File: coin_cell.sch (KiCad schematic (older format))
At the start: 11 parts, among them J1 Barrel_Jack, U1 NC7SZ14-D, U2 TPS61222

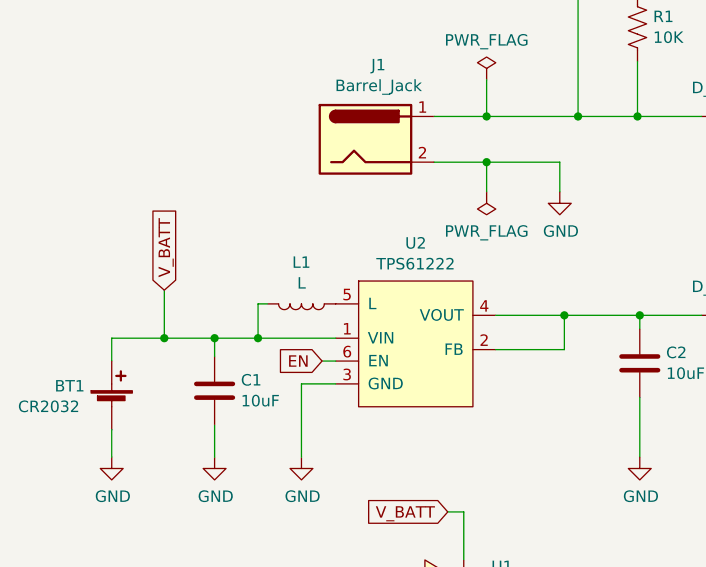
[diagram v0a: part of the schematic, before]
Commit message: Added sc-70-5 footprint and sot23-5 footprint
- assigned footprints to symbols
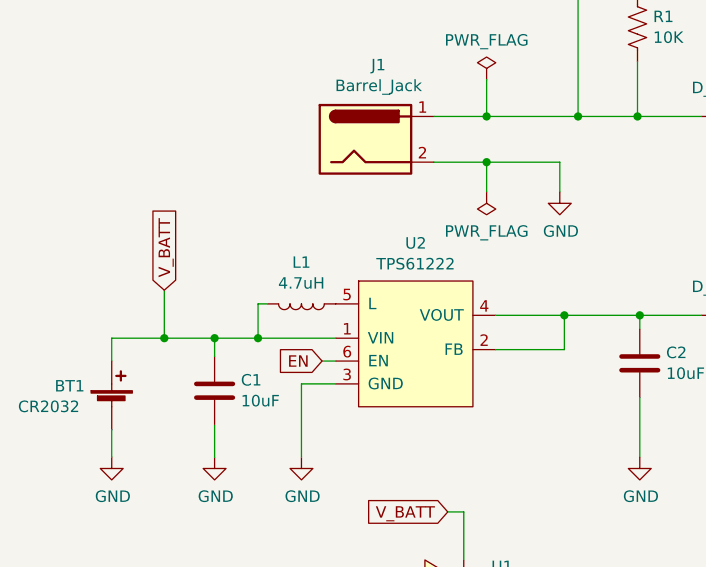
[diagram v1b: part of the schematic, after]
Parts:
- BT1: footprint (none) -> digikey-footprints:Battery_Holder_Coin_2032_BS-7
- C1, C2, C3: footprint (none) -> Capacitor_SMD:C_0805_2012Metric_Pad1.15x1.40mm_HandSolder
- D1, D2: footprint (none) -> Diode_SMD:D_0805_2012Metric_Pad1.15x1.40mm_HandSolder
- J1: footprint (none) -> digikey-footprints:Barrel_Jack_5.5mmODx2.1mmID_PJ-202A
- L1: value L -> 4.7uH; footprint (none) -> Inductor_SMD:L_10.4x10.4_H4.8
- R1: footprint (none) -> Resistor_SMD:R_0805_2012Metric_Pad1.15x1.40mm_HandSolder
- U1: footprint (none) -> coin_cell:SOT-23-5_HandSoldering
- U2: footprint (none) -> Package_TO_SOT_SMD:SOT-363_SC-70-6_Handsoldering
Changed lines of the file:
@@
 EESchema Schematic File Version 4
+LIBS:coin_cell-cache
 EELAYER 29 0
 EELAYER END
@@
 F 0 "U2" H 2620 3385 50  0000 C CNN
 F 1 "TPS61222" H 2620 3294 50  0000 C CNN
-F 2 "" H 2420 2820 50  0001 C CNN
+F 2 "Package_TO_SOT_SMD:SOT-363_SC-70-6_Handsoldering" H 2420 2820 50  0001 C CNN
 F 3 "" H 2420 2820 50  0001 C CNN
 	1    2620 2920
@@
 F 0 "J1" H 2457 2325 50  0000 C CNN
 F 1 "Barrel_Jack" H 2457 2234 50  0000 C CNN
-F 2 "" H 2450 1960 50  0001 C CNN
+F 2 "digikey-footprints:Barrel_Jack_5.5mmODx2.1mmID_PJ-202A" H 2450 1960 50  0001 C CNN
 F 3 "~" H 2450 1960 50  0001 C CNN
 	1    2400 2000
@@
 F 0 "D1" H 4020 1684 50  0000 C CNN
 F 1 "D_Schottky" H 4020 1775 50  0000 C CNN
-F 2 "" H 4020 1900 50  0001 C CNN
+F 2 "Diode_SMD:D_0805_2012Metric_Pad1.15x1.40mm_HandSolder" H 4020 1900 50  0001 C CNN
 F 3 "~" H 4020 1900 50  0001 C CNN
 	1    4020 1900
@@
 F 0 "C2" H 3715 3026 50  0000 L CNN
 F 1 "10uF" H 3715 2935 50  0000 L CNN
-F 2 "" H 3638 2830 50  0001 C CNN
+F 2 "Capacitor_SMD:C_0805_2012Metric_Pad1.15x1.40mm_HandSolder" H 3638 2830 50  0001 C CNN
 F 3 "~" H 3600 2980 50  0001 C CNN
 	1    3600 2980
@@
 P 2120 2720
 F 0 "L1" V 1939 2720 50  0000 C CNN
-F 1 "L" V 2030 2720 50  0000 C CNN
-F 2 "" H 2120 2720 50  0001 C CNN
+F 1 "4.7uH" V 2030 2720 50  0000 C CNN
+F 2 "Inductor_SMD:L_10.4x10.4_H4.8" H 2120 2720 50  0001 C CNN
 F 3 "~" H 2120 2720 50  0001 C CNN
 	1    2120 2720
@@
 F 0 "C1" H 1855 3146 50  0000 L CNN
 F 1 "10uF" H 1855 3055 50  0000 L CNN
-F 2 "" H 1778 2950 50  0001 C CNN
+F 2 "Capacitor_SMD:C_0805_2012Metric_Pad1.15x1.40mm_HandSolder" H 1778 2950 50  0001 C CNN
 F 3 "~" H 1740 3100 50  0001 C CNN
 	1    1740 3100
@@
 F 0 "BT1" H 1040 3260 50  0000 L CNN
 F 1 "CR2032" H 880 3170 50  0000 L CNN
-F 2 "" V 1290 3230 50  0001 C CNN
+F 2 "digikey-footprints:Battery_Holder_Coin_2032_BS-7" V 1290 3230 50  0001 C CNN
 F 3 "~" V 1290 3230 50  0001 C CNN
 	1    1290 3170
@@
 F 0 "D2" H 4020 2554 50  0000 C CNN
 F 1 "D_Schottky" H 4020 2645 50  0000 C CNN
-F 2 "" H 4020 2770 50  0001 C CNN
+F 2 "Diode_SMD:D_0805_2012Metric_Pad1.15x1.40mm_HandSolder" H 4020 2770 50  0001 C CNN
 F 3 "~" H 4020 2770 50  0001 C CNN
 	1    4020 2770
@@
 F 0 "U1" H 2950 4410 50  0000 L CNN
 F 1 "NC7SZ14-D" H 2950 4330 50  0000 L CNN
-F 2 "" H 2860 4140 50  0001 C CNN
+F 2 "coin_cell:SOT-23-5_HandSoldering" H 2860 4140 50  0001 C CNN
 F 3 "" H 2860 4140 50  0001 C CNN
 	1    2860 4140
@@
 F 0 "R1" H 3658 1556 50  0000 L CNN
 F 1 "10K" H 3658 1465 50  0000 L CNN
-F 2 "" V 3630 1500 50  0001 C CNN
+F 2 "Resistor_SMD:R_0805_2012Metric_Pad1.15x1.40mm_HandSolder" V 3630 1500 50  0001 C CNN
 F 3 "~" H 3590 1510 50  0001 C CNN
 	1    3590 1510
@@
 F 0 "C3" H 4755 2826 50  0000 L CNN
 F 1 "100uF" H 4755 2735 50  0000 L CNN
-F 2 "" H 4678 2630 50  0001 C CNN
+F 2 "Capacitor_SMD:C_0805_2012Metric_Pad1.15x1.40mm_HandSolder" H 4678 2630 50  0001 C CNN
 F 3 "~" H 4640 2780 50  0001 C CNN
 	1    4640 2780

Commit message: Added reference pcb layout
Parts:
- BT1: footprint digikey-footprints:Battery_Holder_Coin_2032_BS-7 -> coin_cell:S8211R
- C1, C2, C3: footprint Capacitor_SMD:C_0805_2012Metric_Pad1.15x1.40mm_HandSolder -> coin_cell:Capacitor_0805_2012Metric_Pad1.15x1.40mm_HandSolder
- D1, D2: footprint Diode_SMD:D_0805_2012Metric_Pad1.15x1.40mm_HandSolder -> coin_cell:Diode_0805_2012Metric_Pad1.15x1.40mm_HandSolder
- J1: footprint digikey-footprints:Barrel_Jack_5.5mmODx2.1mmID_PJ-202A -> coin_cell:Barrel_Jack_Small_Hole_Type_5.5mmODx2.1mmID_PJ-102A
- R1: footprint Resistor_SMD:R_0805_2012Metric_Pad1.15x1.40mm_HandSolder -> coin_cell:Resistor_0805_2012Metric_Pad1.15x1.40mm_HandSolder
- U1: footprint coin_cell:SOT-23-5_HandSoldering -> coin_cell:SOT-353_SC-70-5_Handsoldering
- U2: footprint Package_TO_SOT_SMD:SOT-363_SC-70-6_Handsoldering -> coin_cell:SOT-363_SC-70-6_Handsoldering
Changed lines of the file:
@@
 F 0 "U2" H 2620 3385 50  0000 C CNN
 F 1 "TPS61222" H 2620 3294 50  0000 C CNN
-F 2 "Package_TO_SOT_SMD:SOT-363_SC-70-6_Handsoldering" H 2420 2820 50  0001 C CNN
+F 2 "coin_cell:SOT-363_SC-70-6_Handsoldering" H 2420 2820 50  0001 C CNN
 F 3 "" H 2420 2820 50  0001 C CNN
 	1    2620 2920
@@
 F 0 "J1" H 2457 2325 50  0000 C CNN
 F 1 "Barrel_Jack" H 2457 2234 50  0000 C CNN
-F 2 "digikey-footprints:Barrel_Jack_5.5mmODx2.1mmID_PJ-202A" H 2450 1960 50  0001 C CNN
+F 2 "coin_cell:Barrel_Jack_Small_Hole_Type_5.5mmODx2.1mmID_PJ-102A" H 2450 1960 50  0001 C CNN
 F 3 "~" H 2450 1960 50  0001 C CNN
 	1    2400 2000
@@
 F 0 "D1" H 4020 1684 50  0000 C CNN
 F 1 "D_Schottky" H 4020 1775 50  0000 C CNN
-F 2 "Diode_SMD:D_0805_2012Metric_Pad1.15x1.40mm_HandSolder" H 4020 1900 50  0001 C CNN
+F 2 "coin_cell:Diode_0805_2012Metric_Pad1.15x1.40mm_HandSolder" H 4020 1900 50  0001 C CNN
 F 3 "~" H 4020 1900 50  0001 C CNN
 	1    4020 1900
@@
 F 0 "C2" H 3715 3026 50  0000 L CNN
 F 1 "10uF" H 3715 2935 50  0000 L CNN
-F 2 "Capacitor_SMD:C_0805_2012Metric_Pad1.15x1.40mm_HandSolder" H 3638 2830 50  0001 C CNN
+F 2 "coin_cell:Capacitor_0805_2012Metric_Pad1.15x1.40mm_HandSolder" H 3638 2830 50  0001 C CNN
 F 3 "~" H 3600 2980 50  0001 C CNN
 	1    3600 2980
@@
 F 0 "C1" H 1855 3146 50  0000 L CNN
 F 1 "10uF" H 1855 3055 50  0000 L CNN
-F 2 "Capacitor_SMD:C_0805_2012Metric_Pad1.15x1.40mm_HandSolder" H 1778 2950 50  0001 C CNN
+F 2 "coin_cell:Capacitor_0805_2012Metric_Pad1.15x1.40mm_HandSolder" H 1778 2950 50  0001 C CNN
 F 3 "~" H 1740 3100 50  0001 C CNN
 	1    1740 3100
@@
 F 0 "BT1" H 1040 3260 50  0000 L CNN
 F 1 "CR2032" H 880 3170 50  0000 L CNN
-F 2 "digikey-footprints:Battery_Holder_Coin_2032_BS-7" V 1290 3230 50  0001 C CNN
+F 2 "coin_cell:S8211R" V 1290 3230 50  0001 C CNN
 F 3 "~" V 1290 3230 50  0001 C CNN
 	1    1290 3170
@@
 F 0 "D2" H 4020 2554 50  0000 C CNN
 F 1 "D_Schottky" H 4020 2645 50  0000 C CNN
-F 2 "Diode_SMD:D_0805_2012Metric_Pad1.15x1.40mm_HandSolder" H 4020 2770 50  0001 C CNN
+F 2 "coin_cell:Diode_0805_2012Metric_Pad1.15x1.40mm_HandSolder" H 4020 2770 50  0001 C CNN
 F 3 "~" H 4020 2770 50  0001 C CNN
 	1    4020 2770
@@
 F 0 "U1" H 2950 4410 50  0000 L CNN
 F 1 "NC7SZ14-D" H 2950 4330 50  0000 L CNN
-F 2 "coin_cell:SOT-23-5_HandSoldering" H 2860 4140 50  0001 C CNN
+F 2 "coin_cell:SOT-353_SC-70-5_Handsoldering" H 2860 4140 50  0001 C CNN
 F 3 "" H 2860 4140 50  0001 C CNN
 	1    2860 4140
@@
 F 0 "R1" H 3658 1556 50  0000 L CNN
 F 1 "10K" H 3658 1465 50  0000 L CNN
-F 2 "Resistor_SMD:R_0805_2012Metric_Pad1.15x1.40mm_HandSolder" V 3630 1500 50  0001 C CNN
+F 2 "coin_cell:Resistor_0805_2012Metric_Pad1.15x1.40mm_HandSolder" V 3630 1500 50  0001 C CNN
 F 3 "~" H 3590 1510 50  0001 C CNN
 	1    3590 1510
@@
 F 0 "C3" H 4755 2826 50  0000 L CNN
 F 1 "100uF" H 4755 2735 50  0000 L CNN
-F 2 "Capacitor_SMD:C_0805_2012Metric_Pad1.15x1.40mm_HandSolder" H 4678 2630 50  0001 C CNN
+F 2 "coin_cell:Capacitor_0805_2012Metric_Pad1.15x1.40mm_HandSolder" H 4678 2630 50  0001 C CNN
 F 3 "~" H 4640 2780 50  0001 C CNN
 	1    4640 2780
